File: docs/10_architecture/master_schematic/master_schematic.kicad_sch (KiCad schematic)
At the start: 13 parts, among them M1 Motor_3phase, M2 Motor_DC, U7 ACS772LCB-050B-PFF-T, U8 INA240A1PWR, U9 ADS131M04IPWR

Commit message: updated README & documentation
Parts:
- added C1, C2: 440AC 15μF, symbol Device:C_45deg
- added C3: C, symbol Device:C
- added U10: SC35VB160S-G, Diode_THT:Diode_Bridge_Comchip_SCVB-L, symbol Diode_Bridge:SC35VB160S-G
- PS1, U1, U2, U3, U4, U5, U6, VFD1: value ~ -> (none)
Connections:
- net at M1.1: now also M1.2 (-), C2.1, C3.1, U10.2, U10.3
- net at M1.3: now also C1.1, C3.2, U10.4
- new net: C1.2, C2.2
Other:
- note added: "1720 rpm should get us our output set up goes to 2500 no load"
- note added: "440AC 15μF"
- moved on the sheet: M1, U7, U8, U9

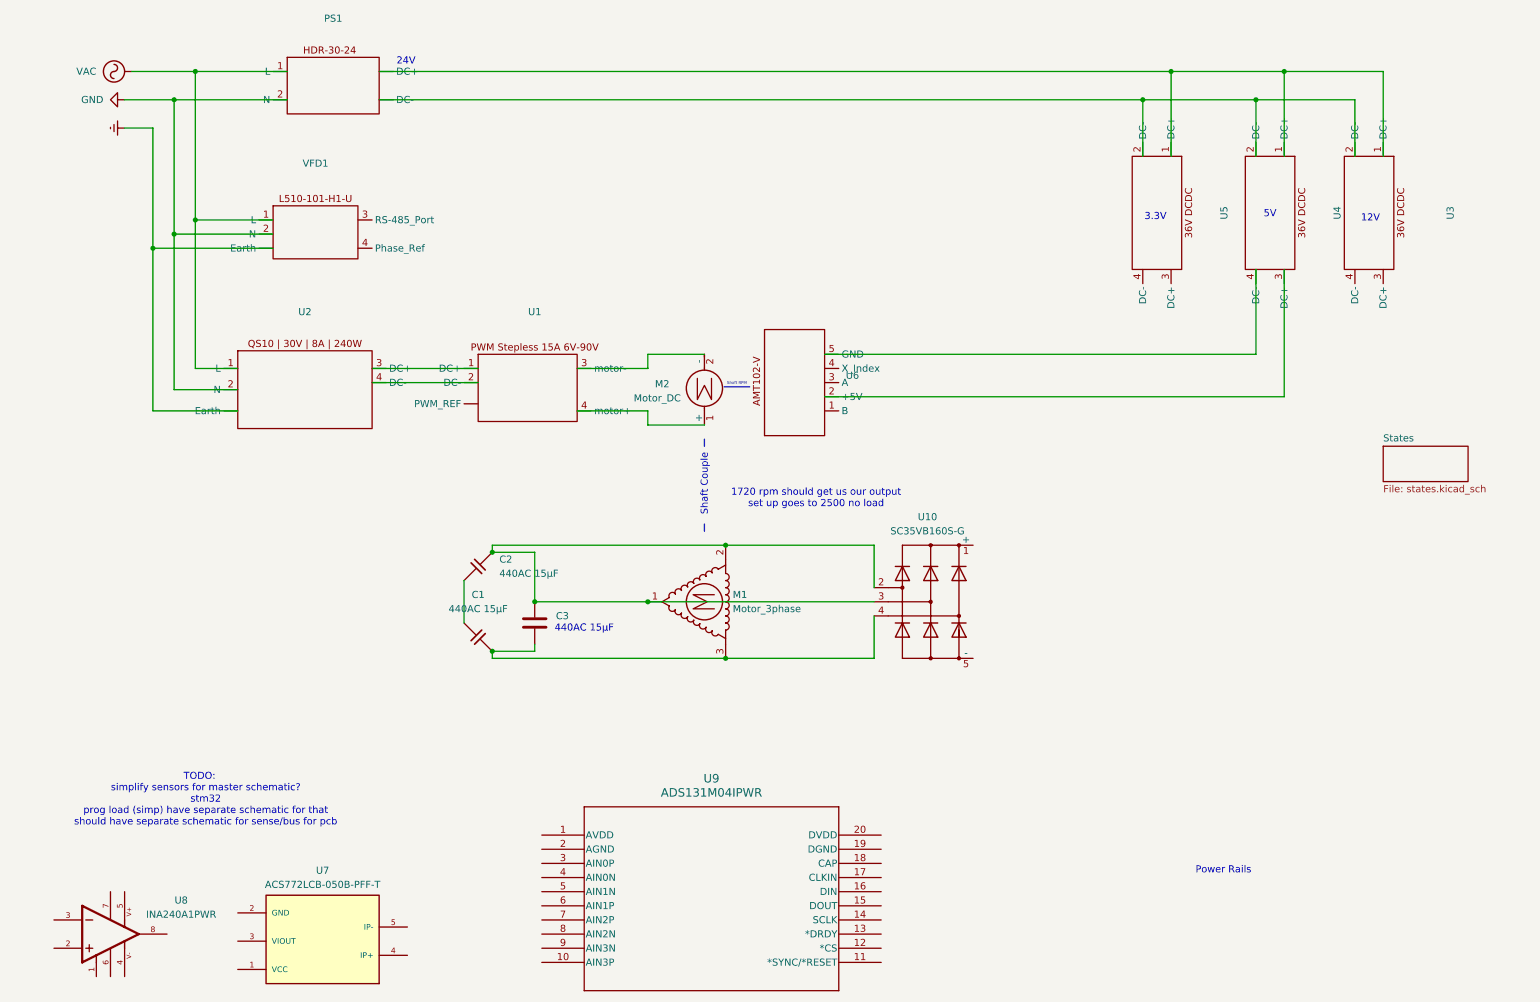
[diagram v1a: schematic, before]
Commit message: updated master schematics, added IV ADC schematic sheet
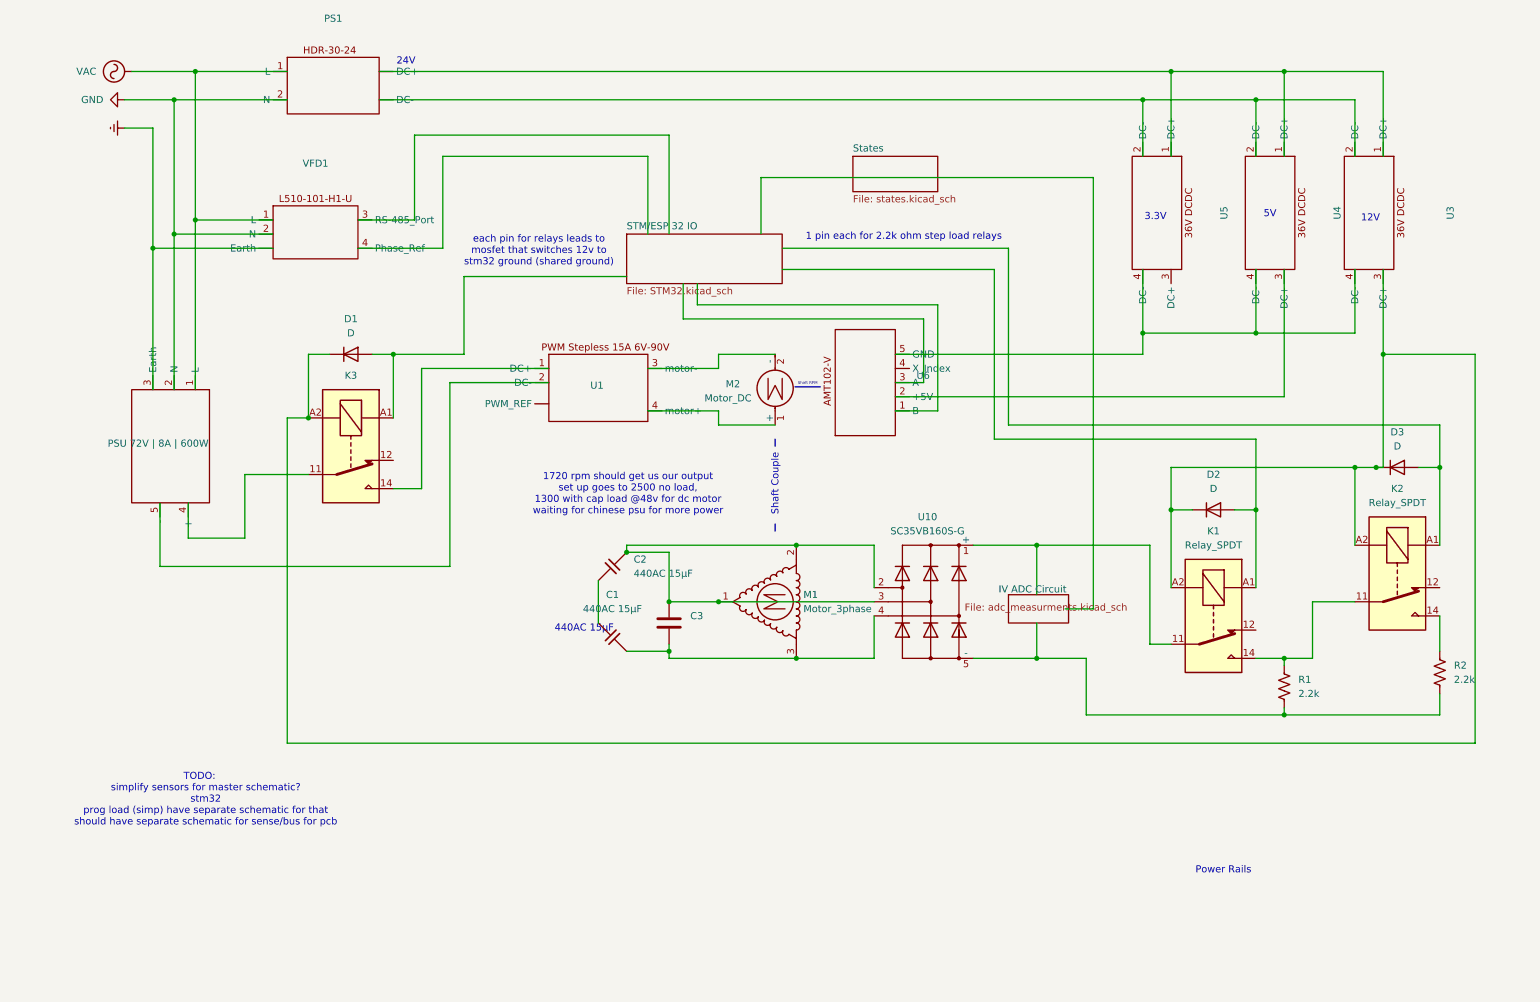
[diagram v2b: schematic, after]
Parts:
- removed U2: (no value), symbol Converter_ACDC:QS10
- removed U7: ACS772LCB-050B-PFF-T, Current_Sense:XDCR_ACS772LCB-050B-PFF-T, symbol Sensor_Current:ACS772LCB-050B-PFF-T
- removed U8: INA240A1PWR, Current_Sense:INA240, symbol Sensor_Current:INA240A1PWR
- removed U9: ADS131M04IPWR, PW20_TEX, symbol 2025-11-11_07-57-10:ADS131M04IPWR
- added D1, D2, D3: D, symbol Device:D
- added K1, K2, K3: Relay_SPDT, symbol Relay:Relay_SPDT
- added PSU 72V | 8A | 600W: (no value), symbol Power_Management:Chinese_PSU_72V_600W
- added R1, R2: 2.2k, symbol Device:R_US
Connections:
- net Earth: now also PSU 72V | 8A | 600W.3 (Earth)
- net GND: now also PSU 72V | 8A | 600W.2 (N)
- net VAC: now also PSU 72V | 8A | 600W.1 (L)
- net at U1.1 (DC+): now also K3.14
- net at U1.2 (DC-): now also PSU 72V | 8A | 600W.5 (-)
- net at U4.4 (DC-), U6.5 (GND): now also U3.4 (DC-), U5.4 (DC-)
- net at U10.1 (+): now also K1.11
- net at U10.5 (-): now also R1.1, R2.2
- net at U3.3 (DC+): now also D1.1 (K), D2.1 (K), D3.1 (K), K1.A2, K2.A2, K3.A2
- new net: K1.14, K2.11, R1.2
- new net: D1.2 (A), K3.A1
- new net: K2.14, R2.1
- new net: D3.2 (A), K2.A1
- new net: K3.11, PSU 72V | 8A | 600W.4 (+)
- new net: D2.2 (A), K1.A1
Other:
- added sheet IV ADC Circuit (adc_measurments.kicad_sch)
- added sheet STM/ESP 32 IO (STM32.kicad_sch)
- note added: "1 pin each for 2.2k ohm step load relays"
- note added: "1720 rpm should get us our output set up goes to 2500 no load, 1300 with cap load @48v for dc motor waiting for chinese psu for more power"
- note added: "each pin for relays leads to mosfet that switches 12v to stm32 ground (shared ground)"
- note removed: "1720 rpm should get us our output set up goes to 2500 no load"
- moved on the sheet: C1, C2, C3, M1, M2, U1, U6

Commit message: updated master schematics
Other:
- moved on the sheet: PSU 72V | 8A | 600W
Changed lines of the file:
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@@
 	(wire
 		(pts
-			(xy 87.63 86.36) (xy 87.63 119.38)
+			(xy 87.63 86.36) (xy 87.63 110.49)
 		)
 		(stroke
@@
 	(wire
 		(pts
+			(xy 96.52 74.93) (xy 121.92 74.93)
+		)
+		(stroke
+			(width 0)
+			(type default)
+		)
+	)
+	(wire
+		(pts
 			(xy 73.66 81.28) (xy 77.47 81.28)
 		)
@@
 	(wire
 		(pts
-			(xy 74.93 30.48) (xy 217.17 30.48)
+			(xy 96.52 90.17) (xy 96.52 74.93)
 		)
 		(stroke
@@
 	(wire
 		(pts
-			(xy 87.63 119.38) (xy 35.56 119.38)
+			(xy 74.93 30.48) (xy 217.17 30.48)
 		)
 		(stroke
@@
 	(wire
 		(pts
-			(xy 34.29 62.23) (xy 34.29 87.63)
+			(xy 34.29 62.23) (xy 34.29 76.2)
 		)
 		(stroke
@@
 	(wire
 		(pts
+			(xy 35.56 96.52) (xy 35.56 110.49)
+		)
+		(stroke
+			(width 0)
+			(type default)
+		)
+	)
+	(wire
+		(pts
 			(xy 167.64 86.36) (xy 172.72 86.36)
 		)
@@
 	(wire
 		(pts
-			(xy 38.1 59.69) (xy 38.1 87.63)
+			(xy 38.1 59.69) (xy 38.1 76.2)
 		)
 		(stroke
@@
 	(wire
 		(pts
-			(xy 237.49 66.04) (xy 237.49 88.9)
+			(xy 105.41 90.17) (xy 96.52 90.17)
 		)
 		(stroke
@@
 	(wire
 		(pts
-			(xy 38.1 35.56) (xy 38.1 59.69)
+			(xy 237.49 66.04) (xy 237.49 88.9)
 		)
 		(stroke
@@
 	(wire
 		(pts
-			(xy 265.43 93.98) (xy 265.43 101.6)
+			(xy 38.1 35.56) (xy 38.1 59.69)
 		)
 		(stroke
@@
 	(wire
 		(pts
-			(xy 217.17 123.19) (xy 217.17 109.22)
+			(xy 265.43 93.98) (xy 265.43 101.6)
 		)
 		(stroke
@@
 	(wire
 		(pts
-			(xy 213.36 133.35) (xy 217.17 133.35)
+			(xy 217.17 123.19) (xy 217.17 109.22)
 		)
 		(stroke
@@
 	(wire
 		(pts
-			(xy 254 101.6) (xy 255.27 101.6)
+			(xy 213.36 133.35) (xy 217.17 133.35)
 		)
 		(stroke
@@
 	(wire
 		(pts
-			(xy 212.09 77.47) (xy 232.41 77.47)
+			(xy 254 101.6) (xy 255.27 101.6)
 		)
 		(stroke
@@
 	(wire
 		(pts
-			(xy 62.23 92.71) (xy 58.42 92.71)
+			(xy 212.09 77.47) (xy 232.41 77.47)
 		)
 		(stroke
@@
 	(wire
 		(pts
-			(xy 40.64 114.3) (xy 50.8 114.3)
+			(xy 62.23 92.71) (xy 58.42 92.71)
 		)
 		(stroke
@@
 	(wire
 		(pts
-			(xy 50.8 114.3) (xy 50.8 102.87)
+			(xy 41.91 57.15) (xy 55.88 57.15)
 		)
 		(stroke
@@
 	(wire
 		(pts
-			(xy 41.91 57.15) (xy 55.88 57.15)
+			(xy 119.38 115.57) (xy 149.86 115.57)
 		)
 		(stroke
@@
 	(wire
 		(pts
-			(xy 119.38 115.57) (xy 149.86 115.57)
+			(xy 132.08 72.39) (xy 132.08 68.58)
 		)
 		(stroke
@@
 	(wire
 		(pts
-			(xy 132.08 72.39) (xy 132.08 68.58)
+			(xy 123.19 91.44) (xy 135.89 91.44)
 		)
 		(stroke
@@
 	(wire
 		(pts
-			(xy 123.19 91.44) (xy 135.89 91.44)
+			(xy 121.92 74.93) (xy 121.92 68.58)
 		)
 		(stroke
@@
 	(wire
 		(pts
+			(xy 40.64 96.52) (xy 40.64 102.87)
+		)
+		(stroke
+			(width 0)
+			(type default)
+		)
+	)
+	(wire
+		(pts
 			(xy 261.62 101.6) (xy 265.43 101.6)
 		)
@@
 	(wire
 		(pts
-			(xy 50.8 102.87) (xy 62.23 102.87)
+			(xy 40.64 102.87) (xy 62.23 102.87)
 		)
 		(stroke
@@
 	(wire
 		(pts
-			(xy 35.56 119.38) (xy 35.56 107.95)
-		)
-		(stroke
-			(width 0)
-			(type default)
-		)
-	)
-	(wire
-		(pts
 			(xy 237.49 135.89) (xy 242.57 135.89)
 		)
@@
 	(wire
 		(pts
-			(xy 40.64 107.95) (xy 40.64 114.3)
+			(xy 35.56 110.49) (xy 87.63 110.49)
 		)
 		(stroke
@@
 	(wire
 		(pts
-			(xy 41.91 57.15) (xy 41.91 87.63)
+			(xy 41.91 57.15) (xy 41.91 76.2)
 		)
 		(stroke
@@
 	(symbol
 		(lib_id "Power_Management:Chinese_PSU_72V_600W")
-		(at 38.1 97.79 270)
+		(at 38.1 86.36 270)
 		(unit 1)
 		(body_style 1)
@@
 		(dnp no)
 		(property "Reference" "PSU 72V | 8A | 600W"
-			(at 26.162 97.282 90)
+			(at 26.162 85.852 90)
 			(show_name no)
 			(do_not_autoplace no)
@@
 		)
 		(property "Value" ""
-			(at 38.1 97.79 0)
+			(at 38.1 86.36 0)
 			(show_name no)
 			(do_not_autoplace no)
@@
 		)
 		(property "Footprint" ""
-			(at 38.1 97.79 0)
+			(at 38.1 86.36 0)
 			(hide yes)
 			(show_name no)
@@
 		)
 		(property "Datasheet" ""
-			(at 38.1 97.79 0)
+			(at 38.1 86.36 0)
 			(hide yes)
 			(show_name no)
@@
 		)
 		(property "Description" ""
-			(at 38.1 97.79 0)
+			(at 38.1 86.36 0)
 			(hide yes)
 			(show_name no)
@@
 	)
 	(sheet
-		(at 160.02 45.72)
+		(at 130.81 39.37)
 		(size 15.24 6.35)
 		(exclude_from_sim no)
@@
 		)
 		(property "Sheetname" "States"
-			(at 160.02 45.0084 0)
+			(at 130.81 38.6584 0)
 			(show_name no)
 			(do_not_autoplace no)
@@
 		)
 		(property "Sheetfile" "states.kicad_sch"
-			(at 160.02 52.6546 0)
+			(at 130.81 46.3046 0)
 			(show_name no)
 			(do_not_autoplace no)

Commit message: created ads131m04 breakout V1
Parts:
- PSU 72V | 8A | 600W1: renamed from PSU 72V | 8A | 600W
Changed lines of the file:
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@@
 		(in_pos_files yes)
 		(dnp no)
-		(property "Reference" "PSU 72V | 8A | 600W"
+		(property "Reference" "PSU 72V | 8A | 600W1"
 			(at 26.162 85.852 90)
 			(show_name no)
@@
 			(project "master_schematic"
 				(path "/161501ba-58a2-4e54-b00f-2c454c29b444"
-					(reference "PSU 72V | 8A | 600W")
+					(reference "PSU 72V | 8A | 600W1")
 					(unit 1)
 				)
